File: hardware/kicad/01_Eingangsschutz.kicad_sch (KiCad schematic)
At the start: 0 parts

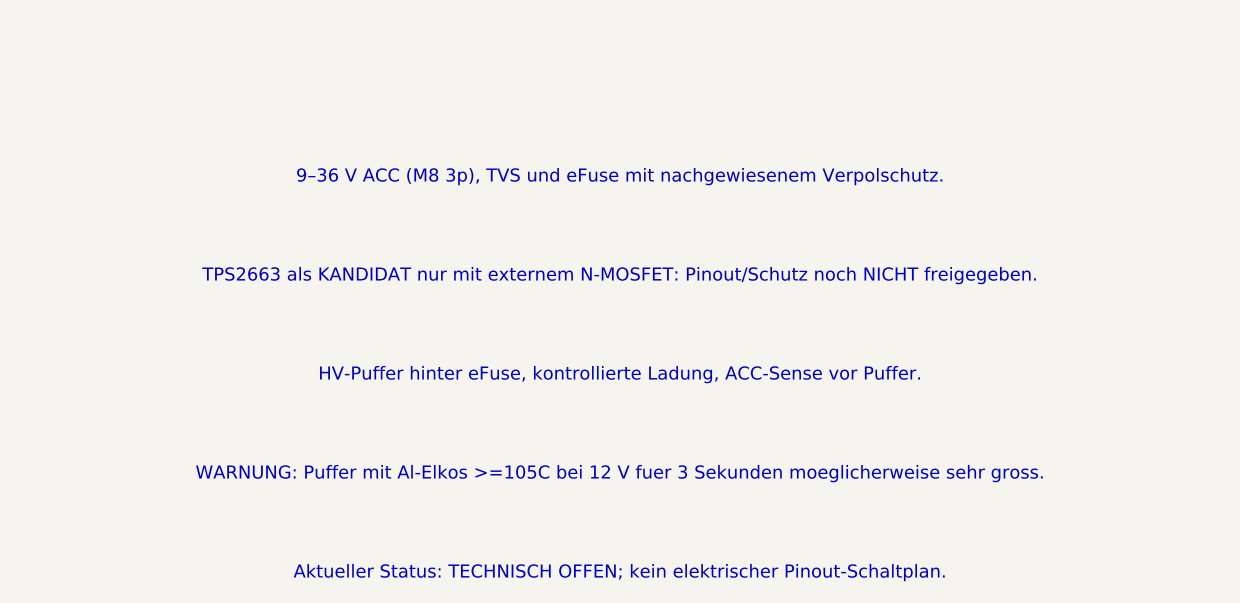
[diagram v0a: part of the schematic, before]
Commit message: hardware: adopt fused ACC/BAT+ microrelay shutdown; drop M8-unplug hold-up requirement
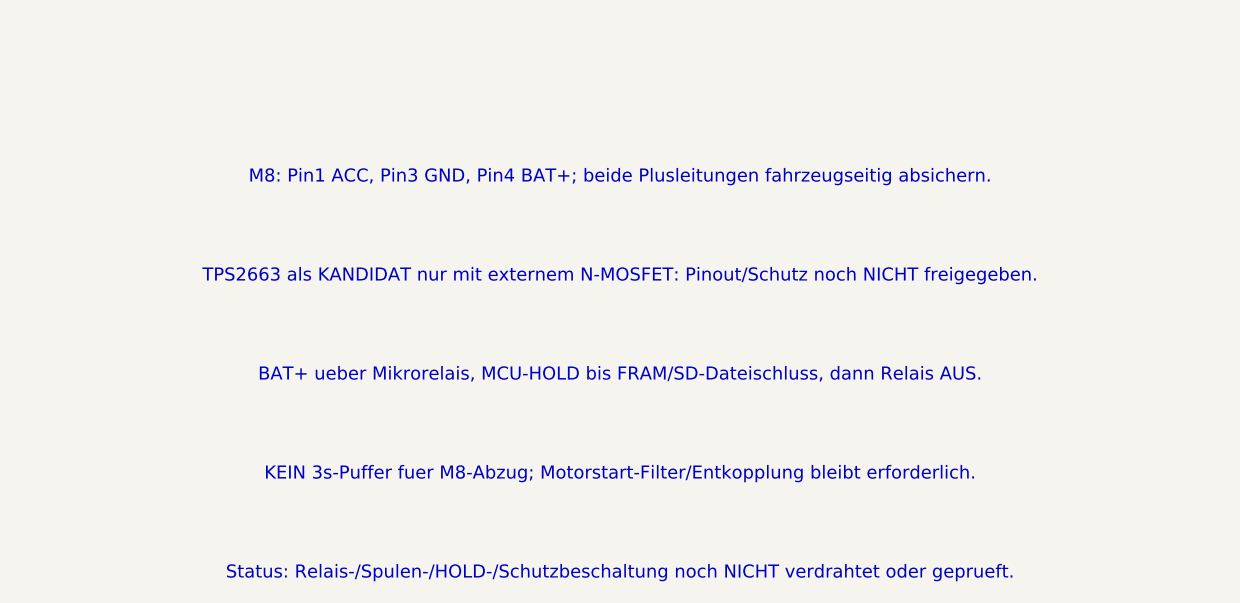
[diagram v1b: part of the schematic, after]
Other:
- note added: "BAT+ ueber Mikrorelais, MCU-HOLD bis FRAM/SD-Dateischluss, dann Relais AUS."
- note added: "KEIN 3s-Puffer fuer M8-Abzug; Motorstart-Filter/Entkopplung bleibt erforderlich."
- note added: "M8: Pin1 ACC, Pin3 GND, Pin4 BAT+; beide Plusleitungen fahrzeugseitig absichern."
- note added: "Status: Relais-/Spulen-/HOLD-/Schutzbeschaltung noch NICHT verdrahtet oder geprueft."
- note removed: "9–36 V ACC (M8 3p), TVS und eFuse mit nachgewiesenem Verpolschutz."
- note removed: "Aktueller Status: TECHNISCH OFFEN; kein elektrischer Pinout-Schaltplan."
- note removed: "HV-Puffer hinter eFuse, kontrollierte Ladung, ACC-Sense vor Puffer."
- note removed: "WARNUNG: Puffer mit Al-Elkos >=105C bei 12 V fuer 3 Sekunden moeglicherweise sehr gross."
- title: TripTracer V1 – Eingangsschutz / eFuse / HV-Puffer -> TripTracer V1 – ACC / BAT+ / Mikrorelais / eFuse
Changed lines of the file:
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@@
 (kicad_sch (version 20250114) (generator "eeschema")
- (paper "A3") (title_block (title "TripTracer V1 – Eingangsschutz / eFuse / HV-Puffer") (date "2026-10-13") (rev "a0 / NOCH NICHT VERDRAHTET"))
+ (paper "A3") (title_block (title "TripTracer V1 – ACC / BAT+ / Mikrorelais / eFuse") (date "2026-10-13") (rev "a0 / NOCH NICHT VERDRAHTET"))
  (text "V1 ARBEITSBLATT / FUNKTION NOCH NICHT SCHALTPLANMAESSIG UMGESETZT." (at 165 35 0) (effects (font (size 2 2))))
- (text "9–36 V ACC (M8 3p), TVS und eFuse mit nachgewiesenem Verpolschutz." (at 165 65 0) (effects (font (size 1.45 1.45))))
+ (text "M8: Pin1 ACC, Pin3 GND, Pin4 BAT+; beide Plusleitungen fahrzeugseitig absichern." (at 165 65 0) (effects (font (size 1.45 1.45))))
 (text "TPS2663 als KANDIDAT nur mit externem N-MOSFET: Pinout/Schutz noch NICHT freigegeben." (at 165 76 0) (effects (font (size 1.45 1.45))))
-(text "HV-Puffer hinter eFuse, kontrollierte Ladung, ACC-Sense vor Puffer." (at 165 87 0) (effects (font (size 1.45 1.45))))
-(text "WARNUNG: Puffer mit Al-Elkos >=105C bei 12 V fuer 3 Sekunden moeglicherweise sehr gross." (at 165 98 0) (effects (font (size 1.45 1.45))))
-(text "Aktueller Status: TECHNISCH OFFEN; kein elektrischer Pinout-Schaltplan." (at 165 109 0) (effects (font (size 1.45 1.45))))
+(text "BAT+ ueber Mikrorelais, MCU-HOLD bis FRAM/SD-Dateischluss, dann Relais AUS." (at 165 87 0) (effects (font (size 1.45 1.45))))
+(text "KEIN 3s-Puffer fuer M8-Abzug; Motorstart-Filter/Entkopplung bleibt erforderlich." (at 165 98 0) (effects (font (size 1.45 1.45))))
+(text "Status: Relais-/Spulen-/HOLD-/Schutzbeschaltung noch NICHT verdrahtet oder geprueft." (at 165 109 0) (effects (font (size 1.45 1.45))))
  (sheet_instances (path "/" (page "2"))) (embedded_fonts no)
 )
